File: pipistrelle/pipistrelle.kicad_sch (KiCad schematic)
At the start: 65 parts, among them J1 C2M, J2 C2F, J3 Eurorack Power, J4 CV1, J5 V/OCT, J6 OUT, J7 CV2, J8 C1M, J9 C1F, U1 SeeeduinoXIAO, U2 MCP6002-xSN, U3 MCP6002-xSN, U4 TL072, U5 LM1117-5.0, U6 LM4040DBZ-10

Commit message: Give it a name: Pipistrelle
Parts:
- D1, D2: value SM4001 -> SM4007PL; footprint Diode_THT:D_DO-41_SOD81_P10.16mm_Horizontal -> Personal:SOD-123FL
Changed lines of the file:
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@@
       (effects (font (size 1.27 1.27)) (justify right))
     )
-    (property "Value" "SM4001" (id 1) (at 245.11 69.8499 90)
-      (effects (font (size 1.27 1.27)) (justify right))
-    )
-    (property "Footprint" "Diode_THT:D_DO-41_SOD81_P10.16mm_Horizontal" (id 2) (at 243.205 68.58 0)
-      (effects (font (size 1.27 1.27)) hide)
-    )
-    (property "Datasheet" "http://www.vishay.com/docs/88503/1n4001.pdf" (id 3) (at 247.65 68.58 0)
+    (property "Value" "SM4007PL" (id 1) (at 245.11 69.8499 90)
+      (effects (font (size 1.27 1.27)) (justify right))
+    )
+    (property "Footprint" "Personal:SOD-123FL" (id 2) (at 243.205 68.58 0)
+      (effects (font (size 1.27 1.27)) hide)
+    )
+    (property "Datasheet" "https://datasheet.lcsc.com/lcsc/1809301215_MDD%EF%BC%88Microdiode-Electronics%EF%BC%89-SM4007PL_C64898.pdf" (id 3) (at 247.65 68.58 0)
       (effects (font (size 1.27 1.27)) hide)
     )
@@
   (symbol (lib_id "Diode:1N4001") (at 247.65 48.26 270) (unit 1)
     (in_bom yes) (on_board yes) (fields_autoplaced)
-    (property "Reference" "D1" (id 0) (at 245.11 46.9899 90)
-      (effects (font (size 1.27 1.27)) (justify right))
-    )
-    (property "Value" "SM4001" (id 1) (at 245.11 49.5299 90)
-      (effects (font (size 1.27 1.27)) (justify right))
-    )
-    (property "Footprint" "Diode_THT:D_DO-41_SOD81_P10.16mm_Horizontal" (id 2) (at 243.205 48.26 0)
-      (effects (font (size 1.27 1.27)) hide)
-    )
-    (property "Datasheet" "http://www.vishay.com/docs/88503/1n4001.pdf" (id 3) (at 247.65 48.26 0)
+    (property "Reference" "D1" (id 0) (at 250.19 46.9899 90)
+      (effects (font (size 1.27 1.27)) (justify left))
+    )
+    (property "Value" "SM4007PL" (id 1) (at 250.19 49.5299 90)
+      (effects (font (size 1.27 1.27)) (justify left))
+    )
+    (property "Footprint" "Personal:SOD-123FL" (id 2) (at 243.205 48.26 0)
+      (effects (font (size 1.27 1.27)) hide)
+    )
+    (property "Datasheet" "https://datasheet.lcsc.com/lcsc/1809301215_MDD%EF%BC%88Microdiode-Electronics%EF%BC%89-SM4007PL_C64898.pdf" (id 3) (at 247.65 48.26 0)
       (effects (font (size 1.27 1.27)) hide)
     )
@@
     )
     (path "/f192a9e3-6913-40e0-99bc-14a77740a619"
-      (reference "D1") (unit 1) (value "SM4001") (footprint "Diode_THT:D_DO-41_SOD81_P10.16mm_Horizontal")
+      (reference "D1") (unit 1) (value "SM4007PL") (footprint "Personal:SOD-123FL")
     )
     (path "/c2a65e83-bd53-4011-981d-1992add6dbe8"
-      (reference "D2") (unit 1) (value "SM4001") (footprint "Diode_THT:D_DO-41_SOD81_P10.16mm_Horizontal")
+      (reference "D2") (unit 1) (value "SM4007PL") (footprint "Personal:SOD-123FL")
     )
     (path "/8ce1e317-c956-4e81-a5ae-69178707098c"

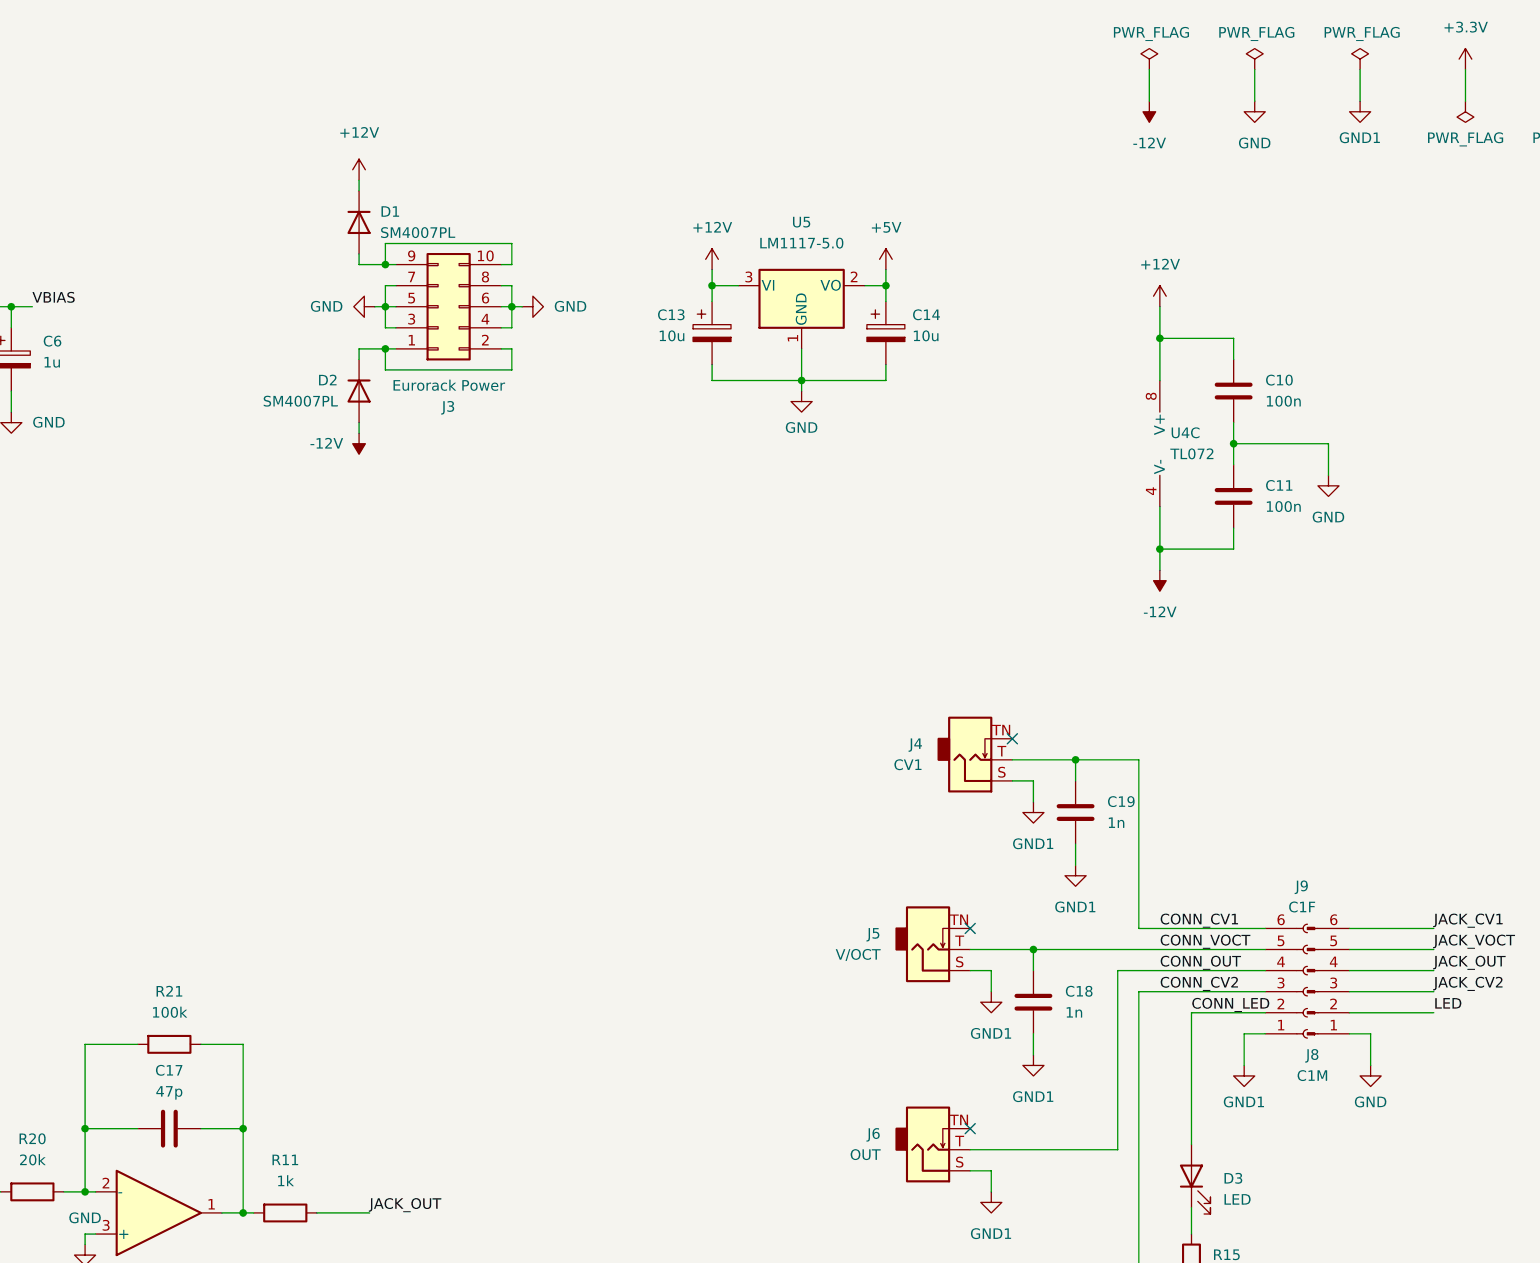
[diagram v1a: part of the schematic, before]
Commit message: Added power caps
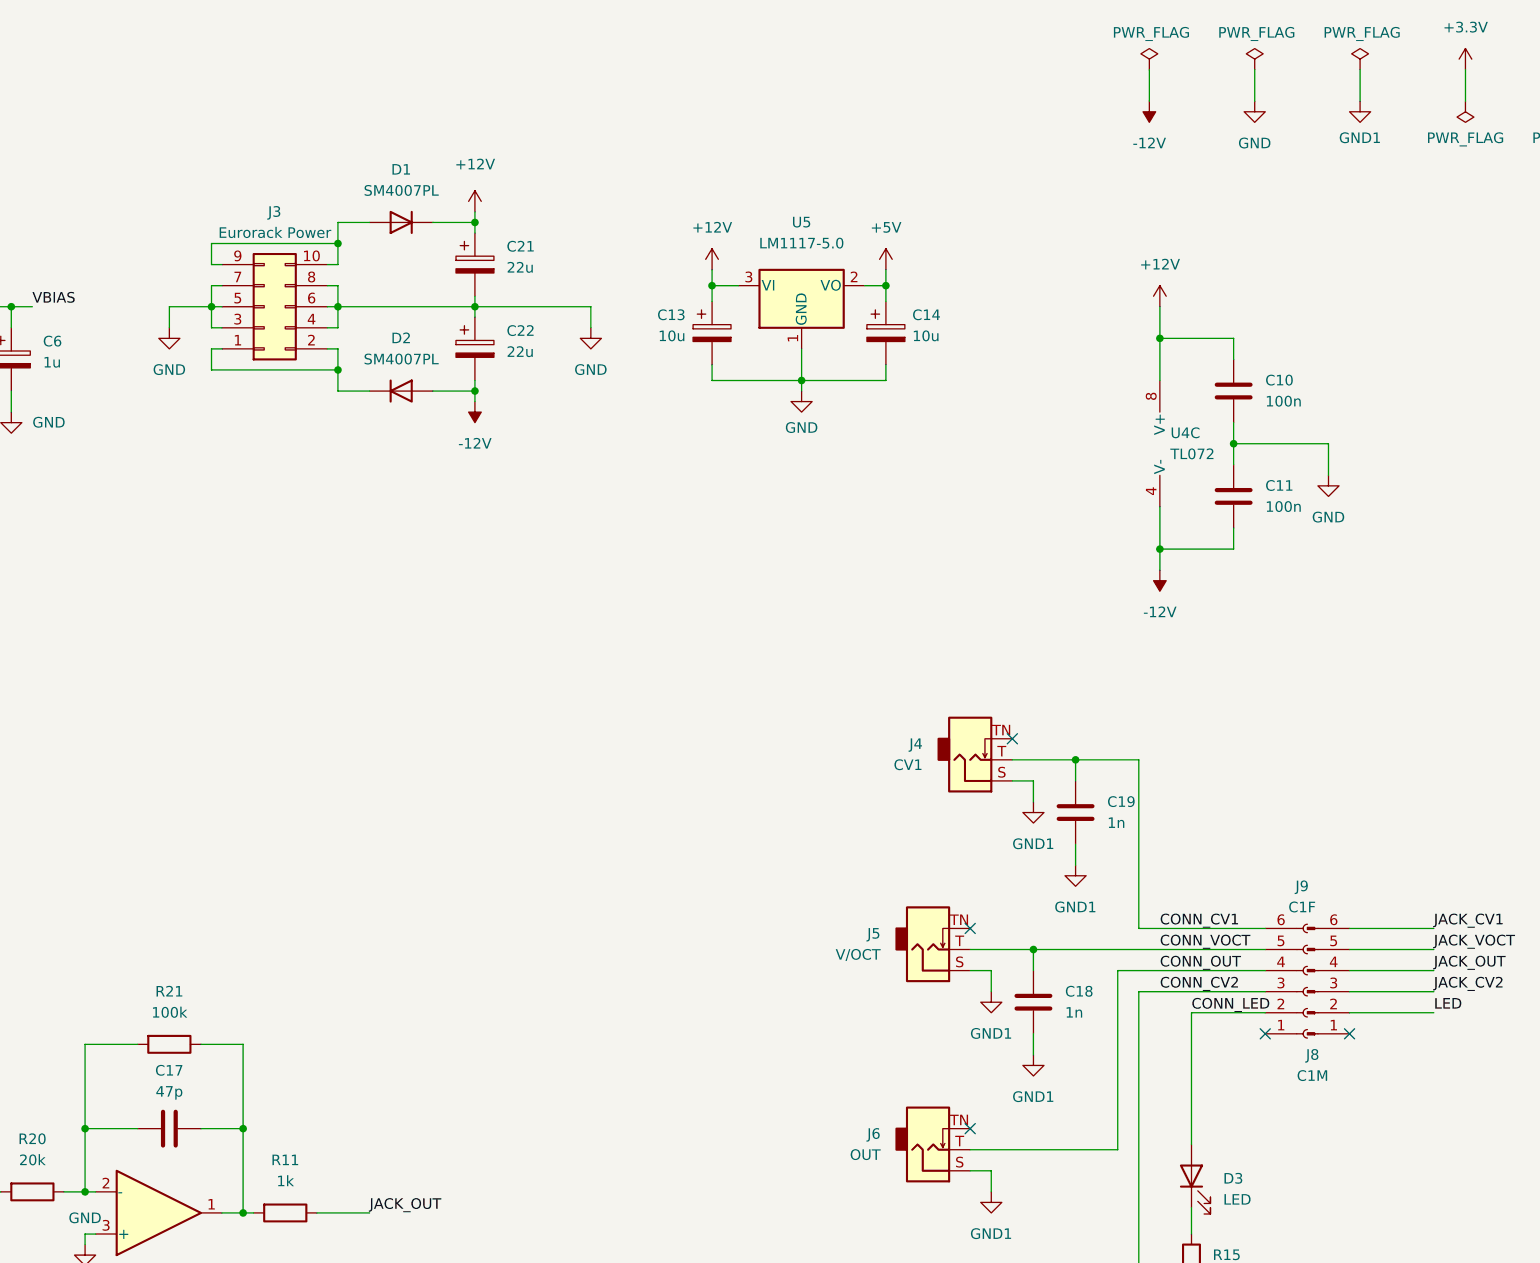
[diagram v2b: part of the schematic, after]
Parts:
- added C21, C22: 22u, Capacitor_SMD:CP_Elec_5x5.9, symbol Device:C_Polarized
- C13, C14: Mouser (none) -> 80-EEV106M035A9BAA
- C6: Mouser (none) -> 667-EEE-HA1H1R0AR
- U6: Mouser (none) -> 926-LM4040DIM3100NPB
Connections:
- net +12V: now also C21.1
- net -12V: now also C22.2
- net GND: now also C21.2, C22.1; no longer J8.1 (Pin_1)
- net GND1: no longer J9.1 (Pin_1)
- no-connect marks 12 -> 14
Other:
- moved on the sheet: D1, D2, J3
